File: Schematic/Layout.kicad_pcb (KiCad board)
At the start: 2 copper layers, 89 x 51 mm, 2 parts

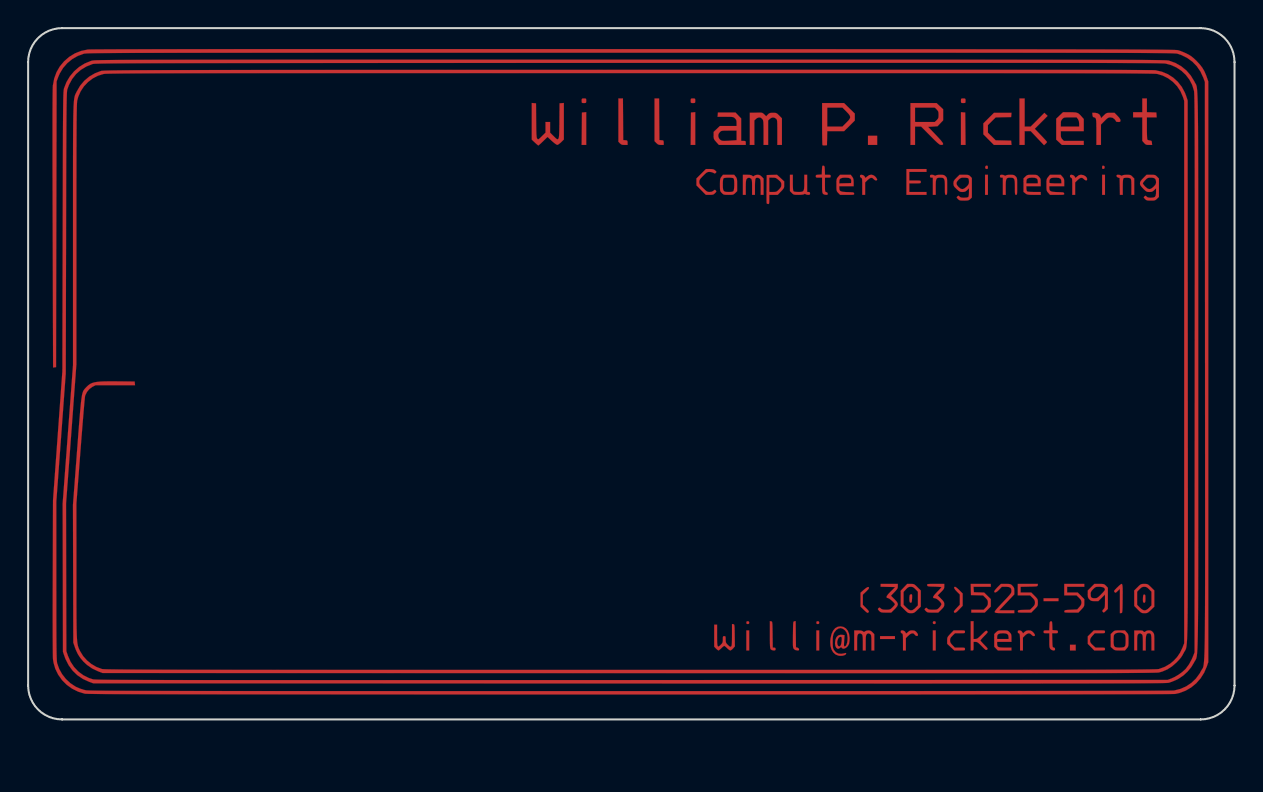
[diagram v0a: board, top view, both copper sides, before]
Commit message: Finished and ordered V1
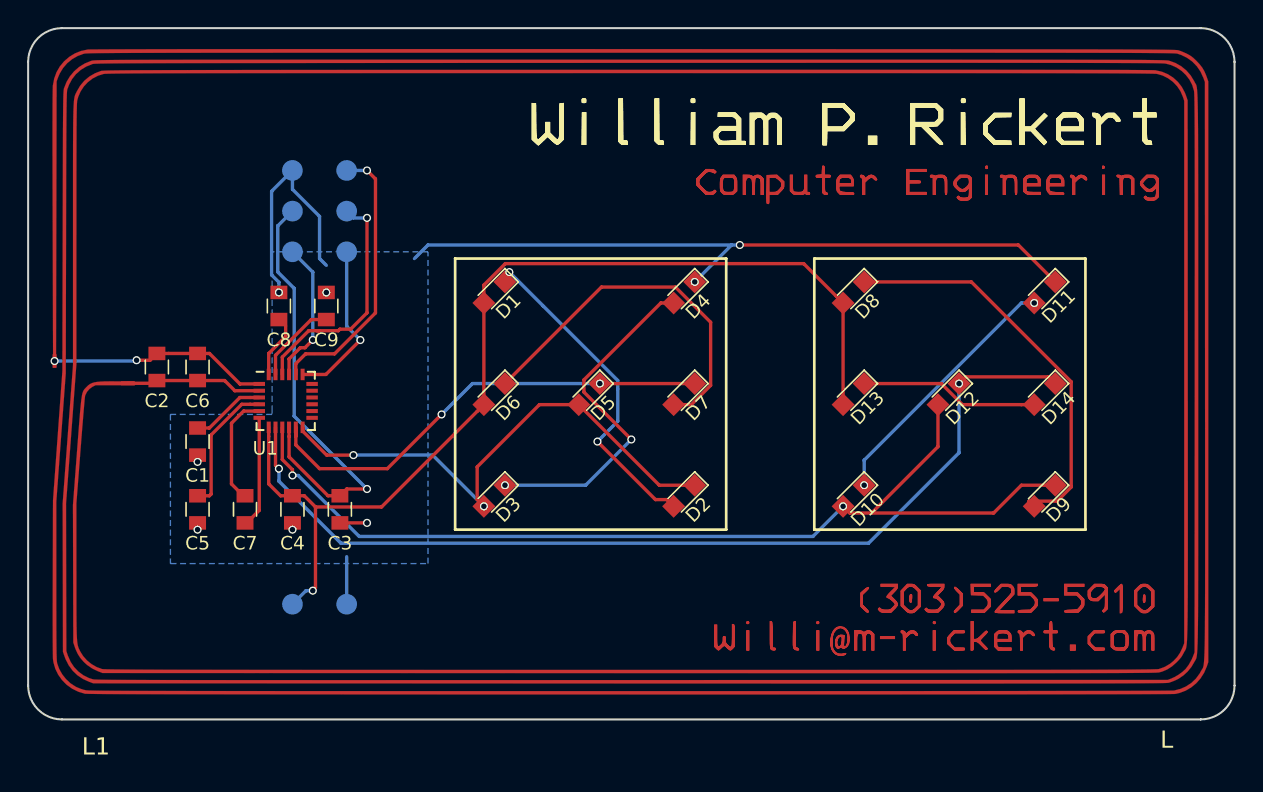
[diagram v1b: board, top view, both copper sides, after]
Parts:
- removed ?: , NFCBusiness:Layout
- removed the G*** at (158.0, 98.5)
- added C1: 2.2uF, Capacitors_SMD:C_0805, F.Cu at (124.5, 104.0)
- added C2: 18pF, Capacitors_SMD:C_0805, F.Cu at (121.5, 98.5)
- added C3: 0.1uF, Capacitors_SMD:C_0805, F.Cu at (135.0, 109.0)
- added C4: 0.1uF, Capacitors_SMD:C_0805, F.Cu at (131.5, 109.0)
- added C5: 0.1uF, Capacitors_SMD:C_0805, F.Cu at (124.5, 109.0)
- added C6: 18pF, Capacitors_SMD:C_0805, F.Cu at (124.5, 98.5)
- added C7: 0.01uF, Capacitors_SMD:C_0805, F.Cu at (128.0, 109.0)
- added C8: 0.1uF, Capacitors_SMD:C_0805, F.Cu at (130.5, 94.0)
- added C9: 0.1uF, Capacitors_SMD:C_0805, F.Cu at (134.0, 94.0)
- added D1: 1-1, LEDs:LED_0805, F.Cu at (146.4, 93.0)
- added D10: 2-3, LEDs:LED_0805, F.Cu at (172.9, 108.0)
- added D11: 2-4, LEDs:LED_0805, F.Cu at (187.0, 93.0)
- added D12: 2-7, LEDs:LED_0805, F.Cu at (179.9, 100.5)
- added D13: 2-5, LEDs:LED_0805, F.Cu at (172.9, 100.5)
- added D14: 2-6, LEDs:LED_0805, F.Cu at (187.0, 100.5)
- added D2: 1-2, LEDs:LED_0805, F.Cu at (160.4, 108.0)
- added D3: 1-3, LEDs:LED_0805, F.Cu at (146.4, 108.0)
- added D4: 1-4, LEDs:LED_0805, F.Cu at (160.4, 93.0)
- added D5: 1-7, LEDs:LED_0805, F.Cu at (153.4, 100.5)
- added D6: 1-5, LEDs:LED_0805, F.Cu at (146.4, 100.5)
- added D7: 1-6, LEDs:LED_0805, F.Cu at (160.4, 100.5)
- added D8: 2-1, LEDs:LED_0805, F.Cu at (172.9, 93.0)
- added D9: 2-2, LEDs:LED_0805, F.Cu at (187.0, 108.0)
- added G*** (x2): LOGO, NFCBusiness:LOGO, F.Cu at (158.0, 98.5)
- added J1: JTAG, NFCBusiness:Jtag, B.Cu at (133.5, 87.0)
- added J2: Power, NFCBusiness:PwrPins, B.Cu at (133.5, 116.0)
- added L1: L, NFCBusiness:Layout, F.Cu at (156.5, 99.0)
- added U1: RF430FRL, Housings_DFN_QFN:QFN-24_4x4mm_Pitch0.5mm_NoMask, F.Cu at (131.0, 101.0)
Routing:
- net VDD: track 0.00 -> 76.7 mm, vias 0 -> 1
- net GND: track 0.00 -> 76.1 mm, vias 0 -> 8
- net P2: track 0.00 -> 74.0 mm, vias 0 -> 2
- net P3: track 0.00 -> 71.5 mm, vias 0 -> 2
- net P0: track 0.00 -> 39.5 mm, vias 0 -> 2
- net P1: track 0.00 -> 34.7 mm, vias 0 -> 2
- net RST: track 0.00 -> 33.0 mm, vias 0 -> 1
- net Net-(D8-Pad1): track 0.00 -> 30.2 mm
- net Net-(D6-Pad1): track 0.00 -> 27.2 mm
- net Net-(D3-Pad1): track 0.00 -> 25.5 mm, vias 0 -> 2
- net Net-(D1-Pad1): track 0.00 -> 24.9 mm, vias 0 -> 2
- net P6: track 0.00 -> 20.5 mm, vias 0 -> 1
- net Net-(D10-Pad1): track 0.00 -> 19.2 mm, vias 0 -> 2
- net P4: track 0.00 -> 17.8 mm, vias 0 -> 1
- net Net-(C2-Pad1): track 0.00 -> 16.3 mm, vias 0 -> 2
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- added copper zone on B.Cu, net GND

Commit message: Added JLC customer id location
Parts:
- removed the G*** at (158.0, 98.5) (x2)
- added G*** (x2): LOGO, NFCBusiness:LOGO, F.Cu at (158.0, 98.5)
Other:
- board text added: "JLCJLCJLCJLC"
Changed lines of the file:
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@@
   (general
     (thickness 1.6)
-    (drawings 17)
+    (drawings 18)
     (tracks 227)
     (zones 0)
@@
     )
   )
+  (gr_text JLCJLCJLCJLC (at 156.464 123.444) (layer B.SilkS)
+    (effects (font (size 0.85 1.5) (thickness 0.2125)) (justify mirror))
+  )
   (gr_line (start 143.5 110.5) (end 163.5 110.5) (layer F.SilkS) (width 0.2))

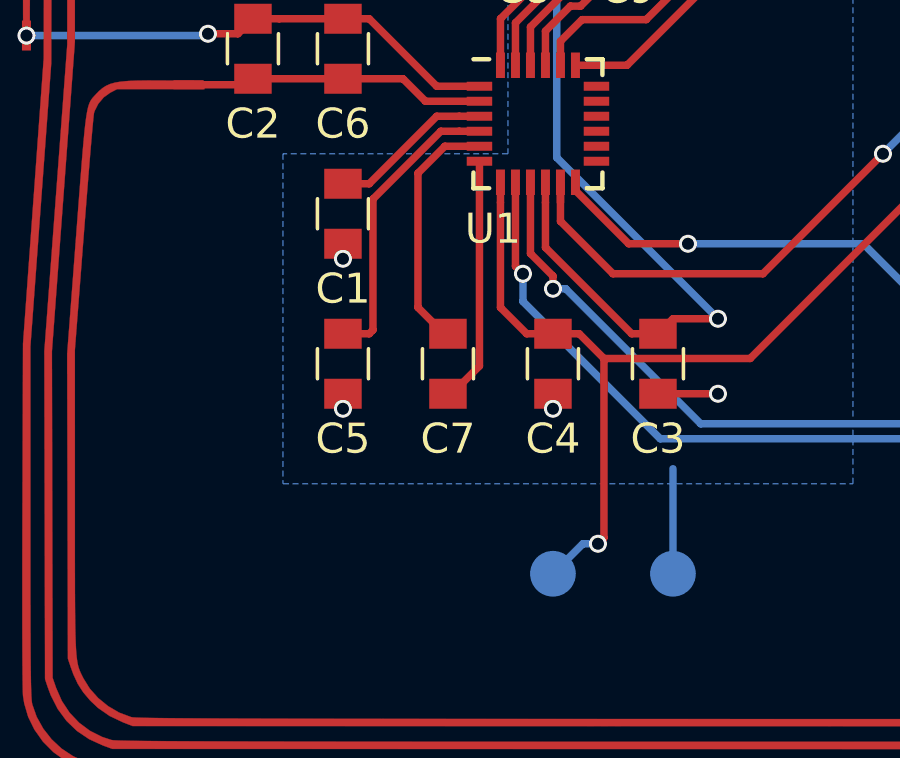
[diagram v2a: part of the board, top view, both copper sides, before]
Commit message: Changed programming footprint to use VDDSW
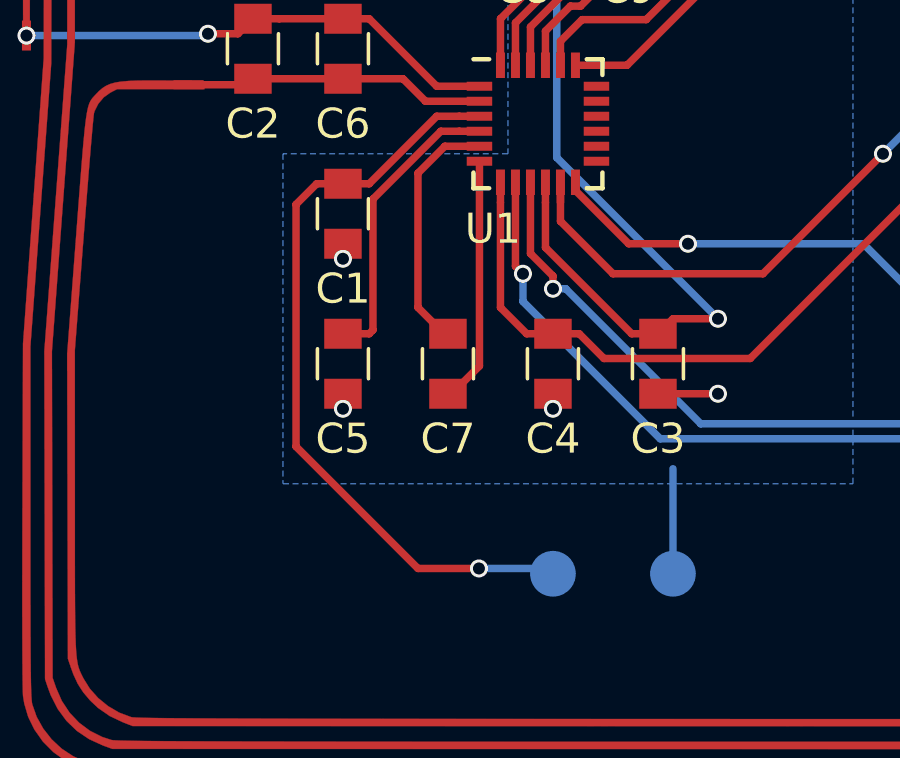
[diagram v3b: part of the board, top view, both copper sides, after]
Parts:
- removed the G*** at (158.0, 98.5) (x2)
- added G*** (x2): LOGO, NFCBusiness:LOGO, F.Cu at (158.0, 98.5)
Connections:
- C1 pad 1: Net-(C1-Pad1) -> VDDA
- J2 pad 2: VDD -> VDDA
- U1 pad 3: Net-(C1-Pad1) -> VDDA
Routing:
- net VDDA: track 0.00 -> 25.7 mm, vias 0 -> 1
- net VDD: track 76.7 -> 68.6 mm, vias 1 -> 0
- net Net-(C1-Pad1): track 5.48 -> 0.00 mm

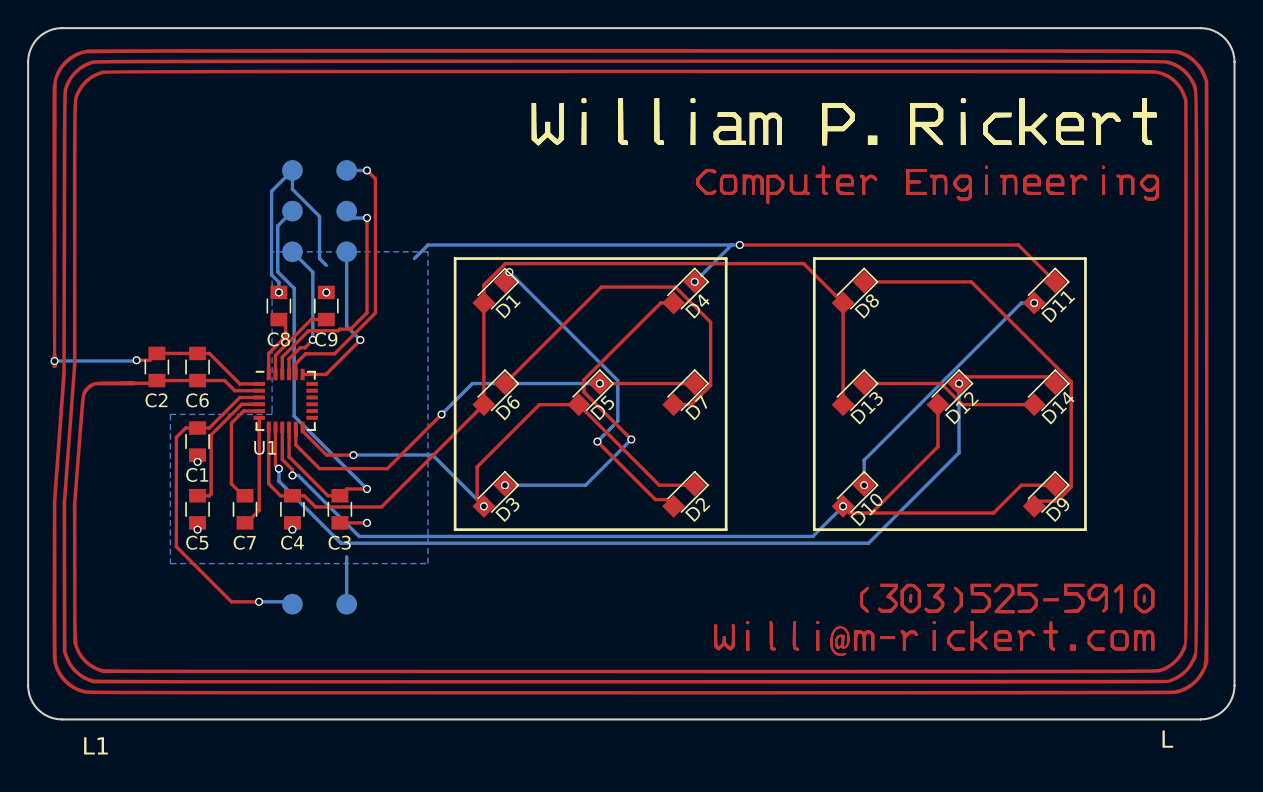
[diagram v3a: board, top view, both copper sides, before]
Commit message: Changed pcb antenna to match proper inductance
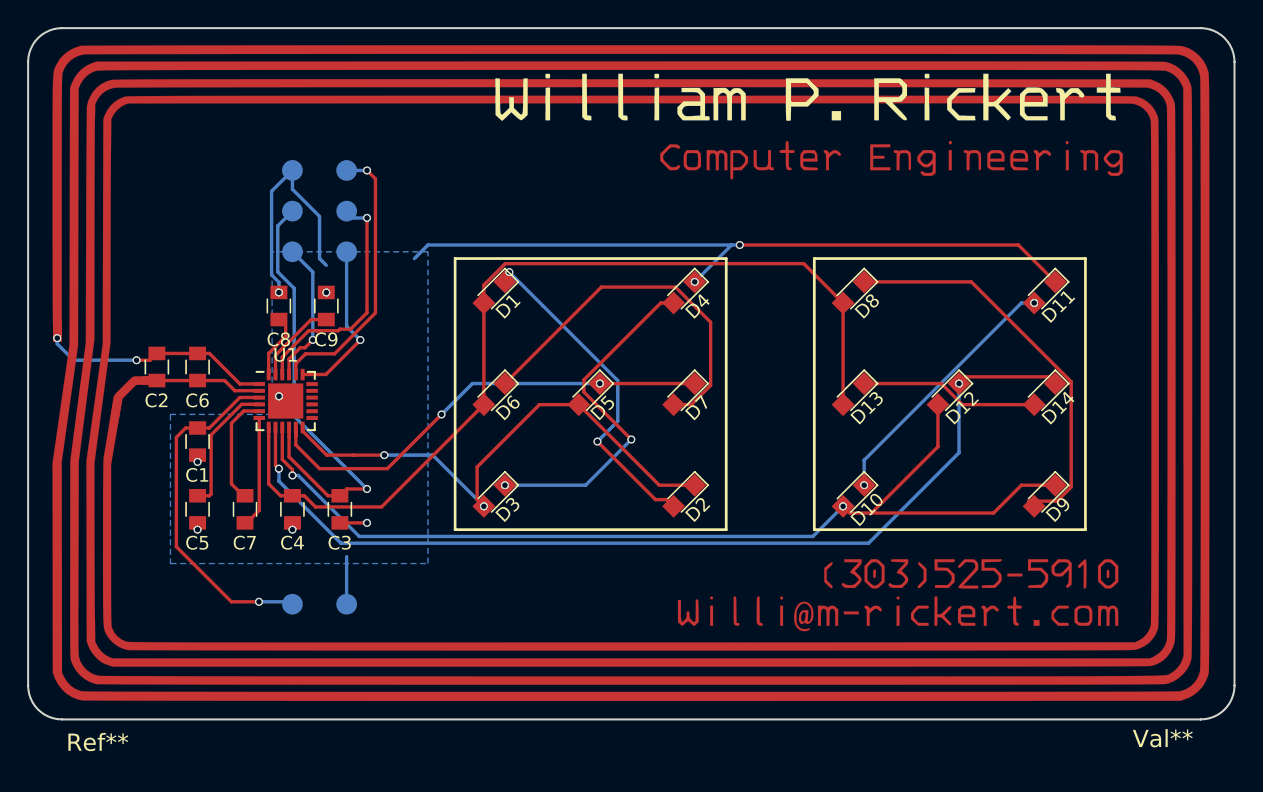
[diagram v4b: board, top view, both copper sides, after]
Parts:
- removed the G*** at (158.0, 98.5) (x2)
- removed L1: L, NFCBusiness:Layout
- added G***: LOGO, NFCBusiness:LOGO, F.Cu at (155.3, 96.7)
- added Ref**: Val**, NFCBuisness:Layout-v2, F.Cu at (156.2, 98.7)
- U1: footprint Housings_DFN_QFN:QFN-24_4x4mm_Pitch0.5mm_NoMask -> Housings_DFN_QFN:QFN-24-1EP_4x4mm_Pitch0.5mm
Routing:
- net Net-(C2-Pad2): track 10.1 -> 12.5 mm
- net Net-(C2-Pad1): track 16.3 -> 17.0 mm
- net (no net): vias 0 -> 1
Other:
- board text added: "V2"
- board text removed: "V1"

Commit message: Played with graphics
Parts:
- removed G***: LOGO, NFCBusiness:LOGO
- added ?: , NFCBuisness:Name, F.Cu at (170.5, 77.0)
- added ?: , NFCBuisness:Rank, F.Cu at (172.1, 81.3)
- added ?: , NFCBuisness:Bottom, F.Cu at (177.2, 114.7)
